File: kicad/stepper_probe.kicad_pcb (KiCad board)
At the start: 2 copper layers, 33 x 42 mm, 44 parts, among them J1 Conn_01x04_Male, J2 Conn_01x04_Male, J3 BAT, J4 Serial Port, J5 SWD, J6 BAT, M1 Motor, SW1 SW_Push, U1 TMCS1108A4BQDT, U2 TMCS1108A4BQDT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

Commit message: Production files with JLCPCB order.
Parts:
- D1, D3: value LED -> LED R
- D2: value LED -> LED Y
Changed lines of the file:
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@@
       (effects (font (size 1 1) (thickness 0.15)))
     )
-    (fp_text value LED (at 0 1.17) (layer F.Fab)
+    (fp_text value "LED R" (at 0 1.17) (layer F.Fab)
       (effects (font (size 1 1) (thickness 0.15)))
     )
@@
       (effects (font (size 1 1) (thickness 0.15)))
     )
-    (fp_text value LED (at 0 1.17 90) (layer F.Fab)
+    (fp_text value "LED Y" (at 0 1.17 90) (layer F.Fab)
       (effects (font (size 1 1) (thickness 0.15)))
     )
@@
       (effects (font (size 1 1) (thickness 0.15)))
     )
-    (fp_text value LED (at 0 1.17 90) (layer F.Fab)
+    (fp_text value "LED R" (at 0 1.17 90) (layer F.Fab)
       (effects (font (size 1 1) (thickness 0.15)))
     )

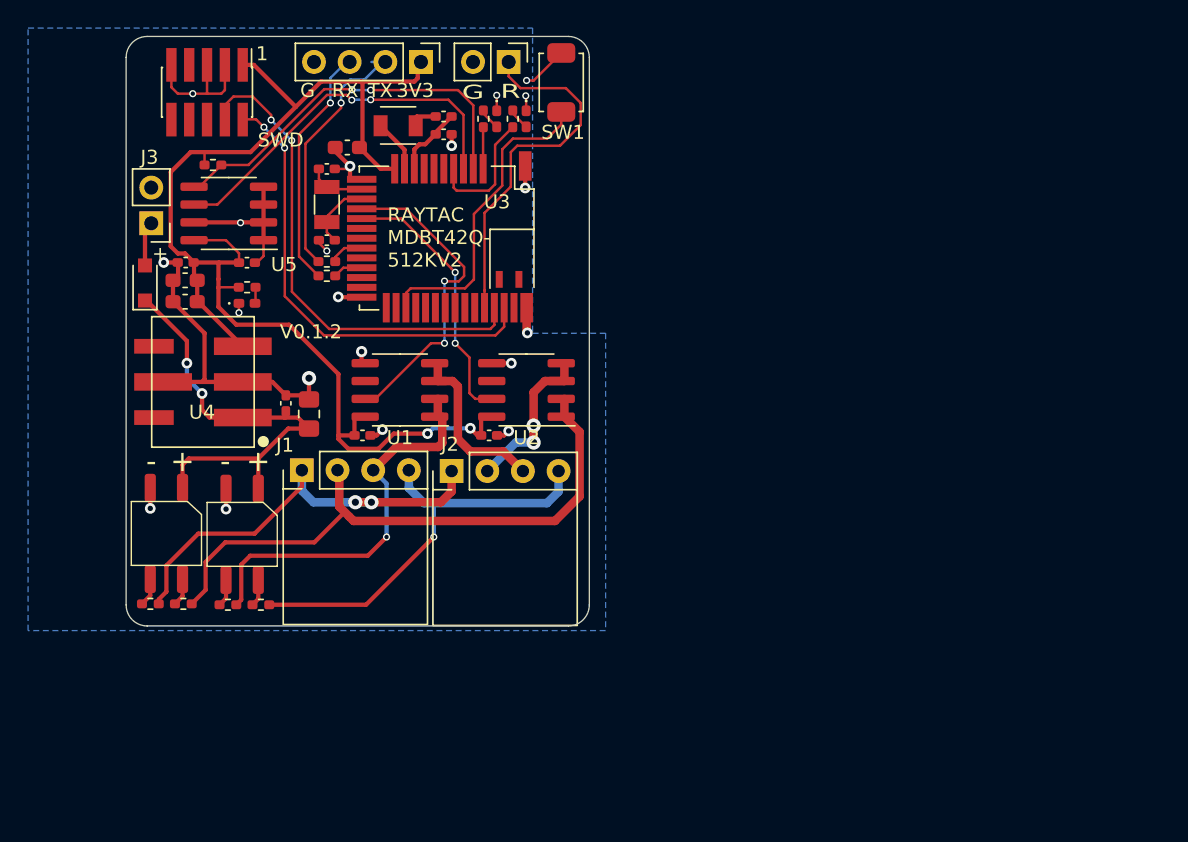
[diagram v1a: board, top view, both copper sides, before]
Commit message: Added calibration battery pads.
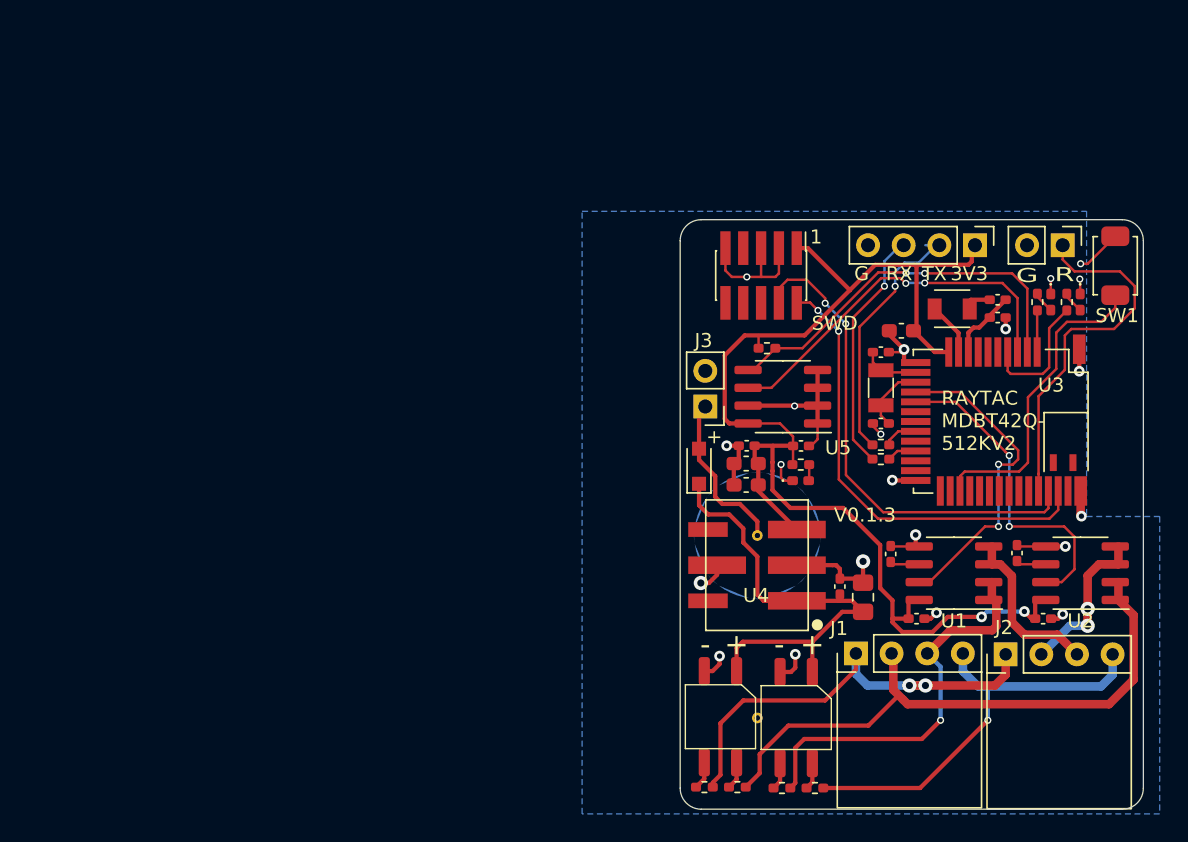
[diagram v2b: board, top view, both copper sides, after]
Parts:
- added C13: DNI, stepper_probe:C_0402_1005Metric_Pad0.74x0.62mm_HandSolder, F.Cu at (163.5, 94.8)
- added C14: DNI, stepper_probe:C_0402_1005Metric_Pad0.74x0.62mm_HandSolder, F.Cu at (154.5, 94.9)
- added J7: Conn_01x01_Female, stepper_probe:BAT_PLUS_PAD, F.Cu at (145.0, 93.6)
- added J8: Conn_01x01_Female, stepper_probe:BAT_MINUS_PAD, F.Cu at (145.0, 106.6)
- moved C9 42.0 mm to (144.2, 87.2)
- moved C10 42.0 mm to (144.2, 88.4)
- moved C11 42.0 mm to (144.2, 90.0)
- moved SW1 41.6 mm to (170.5, 74.3)
- moved D4 41.6 mm to (147.7, 106.5)
- moved C2 41.6 mm to (155.2, 79.0)
- moved C3 41.6 mm to (153.8, 80.5)
- moved C4 41.6 mm to (165.3, 99.5)
- moved C5 41.6 mm to (153.8, 85.6)
- moved J3 41.6 mm to (141.3, 84.4)
- moved J4 41.6 mm to (160.5, 72.9)
- moved L3 41.6 mm to (162.1, 76.8)
- moved R1 41.6 mm to (143.5, 111.5)
- moved R6 41.6 mm to (164.9, 76.9)
- moved R8 41.6 mm to (153.8, 87.1)
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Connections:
- net Net-(D6-Pad2) renamed /BAT+
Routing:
- net /BAT+: track 3.44 -> 12.1 mm
- net /CHB: track 18.7 -> 22.9 mm
- net Net-(C7-Pad1): track 32.3 -> 34.7 mm, vias 2 -> 0
- net Net-(C13-Pad2): track 0.00 -> 2.15 mm
- net Net-(C14-Pad2): track 0.00 -> 2.10 mm
- net +3V3: track 93.6 -> 91.7 mm
- net /STEPPER1: track 31.5 -> 32.6 mm
- net GND: track 69.0 -> 70.0 mm, vias 20 -> 21
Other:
- board text added: "9V BAT ZERO CALIB."
- board text added: "V0.1.3"
- board text removed: "V0.1.2"

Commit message: Added configuration resistors.
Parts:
- added R11: DNP, stepper_probe:R_0402_1005Metric_Pad0.72x0.64mm_HandSolder, F.Cu at (153.7, 89.4)
- added R12: DNP, stepper_probe:R_0402_1005Metric_Pad0.72x0.64mm_HandSolder, F.Cu at (153.7, 90.5)
- moved R9 0.12 mm to (153.7, 88.1)
- moved C3 0.11 mm to (153.7, 80.5)
- moved C5 0.11 mm to (153.7, 85.6)
- moved R8 0.11 mm to (153.7, 87.1)
- moved Y1 0.11 mm to (153.7, 83.0)
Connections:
- U3 pad 22: Net-(U3-Pad22) -> /CFG1
- U3 pad 23: Net-(U3-Pad23) -> /CFG2
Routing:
- net GND: track 70.0 -> 74.6 mm
- net /CFG2: track 0.00 -> 3.00 mm
- net /CFG1: track 0.00 -> 2.72 mm
- net /SWDCLK: track 35.2 -> 35.9 mm
- net /SWDDIO: track 32.8 -> 33.4 mm
- net +3V3: track 91.7 -> 91.2 mm

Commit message: Moved SOIC footprint to local library. Before rotating for JLCPCB.
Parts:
- U1, U2: value TMCS1108A4BQDT -> CC6920BSO-5A; footprint Package_SO:SOIC-8_3.9x4.9mm_P1.27mm -> stepper_probe:SOIC-8_LCPCB_ROT
- U5: footprint Package_SO:SOIC-8_3.9x4.9mm_P1.27mm -> stepper_probe:SOIC-8_LCPCB_ROT

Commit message: Rotated footprints for JLCPCB orientation.
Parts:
- turned J5 to 180 degrees
- turned U1 to 90 degrees
- turned U2 to 90 degrees
- turned U4 to 90 degrees
- turned U5 to 90 degrees

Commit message: Assorted tweaks.
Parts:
- added R13: 0R, stepper_probe:R_0402_1005Metric_Pad0.72x0.64mm_HandSolder, F.Cu at (150.4, 99.6)
- added R14: 0R, stepper_probe:R_0402_1005Metric_Pad0.72x0.64mm_HandSolder, F.Cu at (146.4, 87.8)
- added R15: 0R, stepper_probe:R_0402_1005Metric_Pad0.72x0.64mm_HandSolder, F.Cu at (155.3, 77.4)
- moved J3 2.61 mm to (141.3, 81.8), turned to 0 degrees
- moved C8 0.68 mm to (150.9, 97.9)
- moved C7 0.30 mm to (152.7, 98.2)
- moved D3 0.20 mm to (148.1, 89.5), turned to 180 degrees
- moved R5 0.20 mm to (148.2, 88.3)
- moved C12 0.06 mm to (148.1, 87.2)
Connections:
- C10 pad 1: +3V3 -> Net-(C10-Pad1)
- C11 pad 1: +3V3 -> Net-(C10-Pad1)
- C2 pad 1: +3V3 -> Net-(C2-Pad1)
- C9 pad 1: +3V3 -> Net-(C10-Pad1)
- J3 pad 1: /BAT+ -> GND
- J3 pad 2: GND -> /BAT+
- U3 pad 11: +3V3 -> Net-(C2-Pad1)
- U4 pad 1: Net-(C7-Pad1) -> Net-(R13-Pad1)
- U4 pad 3: +3V3 -> Net-(C10-Pad1)
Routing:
- net +3V3: track 91.2 -> 75.8 mm
- net Net-(C10-Pad1): track 0.00 -> 8.85 mm
- net Net-(C2-Pad1): track 0.00 -> 5.75 mm
- net Net-(C7-Pad1): track 34.7 -> 29.5 mm
- net Net-(R13-Pad1): track 0.00 -> 2.95 mm
- net GND: track 74.6 -> 73.2 mm
- net Net-(D3-Pad2): track 1.16 -> 1.71 mm

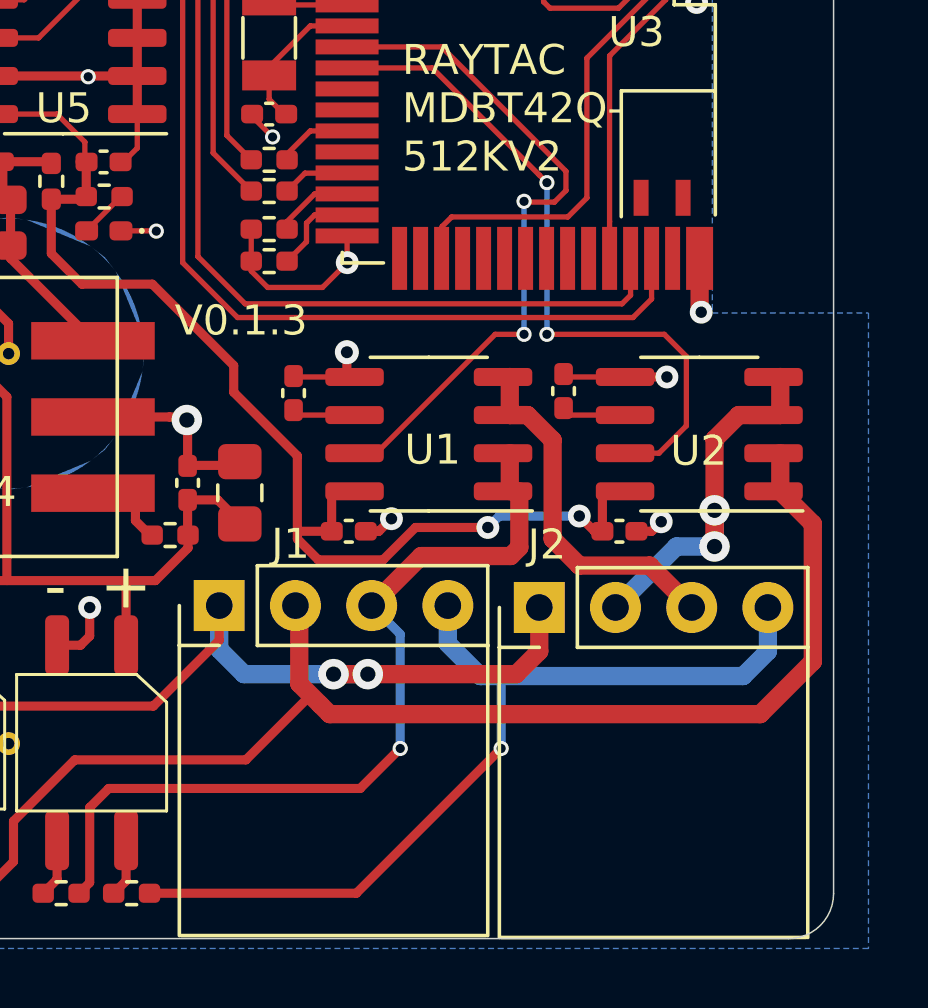
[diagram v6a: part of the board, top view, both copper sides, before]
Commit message: Added the stepper connectors to JLCPCB files.
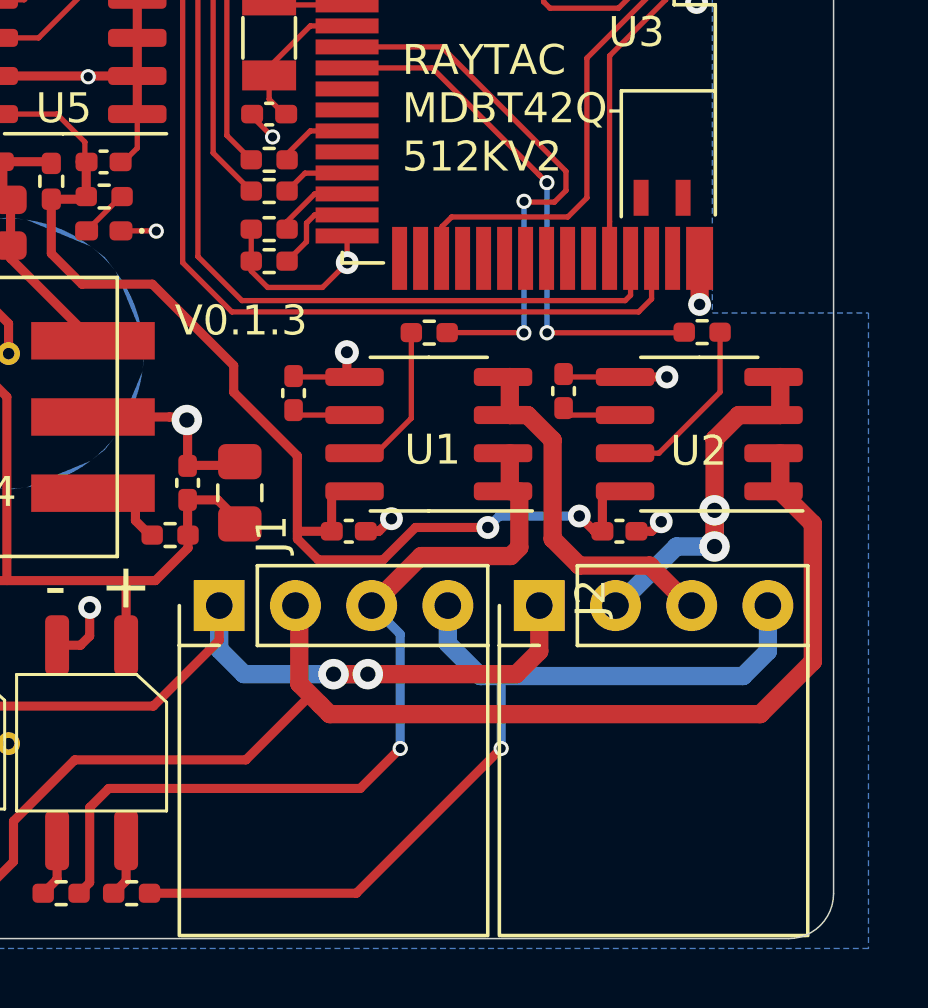
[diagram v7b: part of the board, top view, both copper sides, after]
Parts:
- added R16: 1K, stepper_probe:R_0402_1005Metric_Pad0.72x0.64mm_HandSolder, F.Cu at (159.0, 92.9)
- added R17: 1K, stepper_probe:R_0402_1005Metric_Pad0.72x0.64mm_HandSolder, F.Cu at (168.1, 92.8)
- moved J2 3.81 mm to (166.5, 102.0), turned to 180 degrees
- moved J1 3.81 mm to (155.8, 102.0), turned to 180 degrees
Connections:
- U1 pad 7: /CHA -> Net-(R16-Pad2)
- U2 pad 7: /CHB -> Net-(R17-Pad2)
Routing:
- net Net-(R17-Pad2): track 0.00 -> 6.01 mm
- net Net-(R16-Pad2): track 0.00 -> 5.45 mm
- net /CHB: track 22.9 -> 17.6 mm
- net /CHA: track 23.2 -> 18.1 mm
